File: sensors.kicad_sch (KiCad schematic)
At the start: 17 parts

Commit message: refactor labels U and assigned resistance footprint
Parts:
- R22: footprint (none) -> Resistor_SMD:R_0603_1608Metric
- U4: renamed from U5; value ~ -> SPL06-001
- U5: renamed from U6; value ~ -> ICM-42688-P
- U6: renamed from U8; value ~ -> QMC5883L
- U7: value ~ -> MPU6500
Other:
- moved on the sheet: C30, U5
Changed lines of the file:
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@@
 	(paper "A4")
 	(junction
-		(at 140.97 57.15)
+		(at 163.83 57.15)
 		(diameter 0)
 		(color 0 0 0 0)
 	)
 	(junction
-		(at 140.97 44.45)
+		(at 163.83 44.45)
 		(diameter 0)
 		(color 0 0 0 0)
 	)
 	(junction
-		(at 140.97 60.96)
+		(at 163.83 60.96)
 		(diameter 0)
 		(color 0 0 0 0)
@@
 	)
 	(junction
-		(at 130.81 53.34)
+		(at 153.67 53.34)
 		(diameter 0)
 		(color 0 0 0 0)
@@
 	(wire
 		(pts
-			(xy 140.97 57.15) (xy 140.97 60.96)
+			(xy 163.83 57.15) (xy 163.83 60.96)
 		)
 		(stroke
@@
 	(wire
 		(pts
-			(xy 140.97 45.72) (xy 140.97 44.45)
+			(xy 163.83 45.72) (xy 163.83 44.45)
 		)
 		(stroke
@@
 	(wire
 		(pts
-			(xy 140.97 44.45) (xy 138.43 44.45)
+			(xy 163.83 44.45) (xy 161.29 44.45)
 		)
 		(stroke
@@
 	(wire
 		(pts
-			(xy 142.24 38.1) (xy 144.78 38.1)
+			(xy 165.1 38.1) (xy 167.64 38.1)
 		)
 		(stroke
@@
 	(wire
 		(pts
-			(xy 144.78 60.96) (xy 140.97 60.96)
+			(xy 167.64 60.96) (xy 163.83 60.96)
 		)
 		(stroke
@@
 	(wire
 		(pts
-			(xy 144.78 45.72) (xy 140.97 45.72)
+			(xy 167.64 45.72) (xy 163.83 45.72)
 		)
 		(stroke
@@
 	(wire
 		(pts
-			(xy 130.81 53.34) (xy 144.78 53.34)
+			(xy 153.67 53.34) (xy 167.64 53.34)
 		)
 		(stroke
@@
 	(wire
 		(pts
-			(xy 138.43 57.15) (xy 140.97 57.15)
+			(xy 161.29 57.15) (xy 163.83 57.15)
 		)
 		(stroke
@@
 	(wire
 		(pts
-			(xy 140.97 60.96) (xy 140.97 63.5)
+			(xy 163.83 60.96) (xy 163.83 63.5)
 		)
 		(stroke
@@
 	(wire
 		(pts
-			(xy 140.97 41.91) (xy 140.97 44.45)
+			(xy 163.83 41.91) (xy 163.83 44.45)
 		)
 		(stroke
@@
 	(wire
 		(pts
-			(xy 130.81 53.34) (xy 128.27 53.34)
+			(xy 153.67 53.34) (xy 151.13 53.34)
 		)
 		(stroke
@@
 	(wire
 		(pts
-			(xy 143.51 49.53) (xy 144.78 49.53)
+			(xy 166.37 49.53) (xy 167.64 49.53)
 		)
 		(stroke
@@
 	(wire
 		(pts
-			(xy 144.78 41.91) (xy 140.97 41.91)
+			(xy 167.64 41.91) (xy 163.83 41.91)
 		)
 		(stroke
@@
 	(wire
 		(pts
-			(xy 144.78 57.15) (xy 140.97 57.15)
+			(xy 167.64 57.15) (xy 163.83 57.15)
 		)
 		(stroke
@@
 	(wire
 		(pts
-			(xy 130.81 57.15) (xy 130.81 53.34)
+			(xy 153.67 57.15) (xy 153.67 53.34)
 		)
 		(stroke
@@
 	(global_label "VDD_MCU"
 		(shape input)
-		(at 128.27 53.34 180)
+		(at 151.13 53.34 180)
 		(fields_autoplaced yes)
 		(effects
@@
 		)
 		(property "Intersheetrefs" "${INTERSHEET_REFS}"
-			(at 116.6367 53.34 0)
+			(at 139.4967 53.34 0)
 			(effects
 				(font
@@
 	(global_label "IMU1_SPI4_EXTI2"
 		(shape input)
-		(at 143.51 49.53 180)
+		(at 166.37 49.53 180)
 		(fields_autoplaced yes)
 		(effects
@@
 		)
 		(property "Intersheetrefs" "${INTERSHEET_REFS}"
-			(at 124.5592 49.53 0)
+			(at 147.4192 49.53 0)
 			(effects
 				(font
@@
 	(global_label "SPI4_MISO"
 		(shape input)
-		(at 142.24 38.1 180)
+		(at 165.1 38.1 180)
 		(fields_autoplaced yes)
 		(effects
@@
 		)
 		(property "Intersheetrefs" "${INTERSHEET_REFS}"
-			(at 129.3972 38.1 0)
+			(at 152.2572 38.1 0)
 			(effects
 				(font
@@
 	(symbol
 		(lib_id "power:GND")
-		(at 138.43 44.45 270)
+		(at 161.29 44.45 270)
 		(unit 1)
 		(exclude_from_sim no)
@@
 		(fields_autoplaced yes)
 		(property "Reference" "#PWR026"
-			(at 132.08 44.45 0)
+			(at 154.94 44.45 0)
 			(effects
 				(font
@@
 		)
 		(property "Value" "GND"
-			(at 134.62 44.4499 90)
+			(at 157.48 44.4499 90)
 			(effects
 				(font
@@
 		)
 		(property "Footprint" ""
-			(at 138.43 44.45 0)
+			(at 161.29 44.45 0)
 			(effects
 				(font
@@
 		)
 		(property "Datasheet" ""
-			(at 138.43 44.45 0)
+			(at 161.29 44.45 0)
 			(effects
 				(font
@@
 		)
 		(property "Description" "Power symbol creates a global label with name \"GND\" , ground"
-			(at 138.43 44.45 0)
+			(at 161.29 44.45 0)
 			(effects
 				(font
@@
 		(dnp no)
 		(fields_autoplaced yes)
-		(property "Reference" "U8"
+		(property "Reference" "U6"
 			(at 73.66 99.06 0)
 			(effects
@@
 			)
 		)
-		(property "Value" "~"
+		(property "Value" "QMC5883L"
 			(at 73.66 101.6 0)
 			(effects
@@
 			(project ""
 				(path "/11716af6-0e6e-444b-b738-3f12da23c1a2/8bde1870-17fd-4277-9e11-3b03ad7c1e16"
-					(reference "U8")
+					(reference "U6")
 					(unit 1)
 				)
@@
 	(symbol
 		(lib_id "Device:C")
-		(at 134.62 57.15 90)
+		(at 157.48 57.15 90)
 		(unit 1)
 		(exclude_from_sim no)
@@
 		(dnp no)
 		(property "Reference" "C30"
-			(at 134.62 60.706 90)
+			(at 157.48 60.706 90)
 			(effects
 				(font
@@
 		)
 		(property "Value" "100n"
-			(at 131.064 58.166 90)
+			(at 153.924 58.166 90)
 			(effects
 				(font
@@
 		)
 		(property "Footprint" ""
-			(at 138.43 56.1848 0)
+			(at 161.29 56.1848 0)
 			(effects
 				(font
@@
 		)
 		(property "Datasheet" "~"
-			(at 134.62 57.15 0)
+			(at 157.48 57.15 0)
 			(effects
 				(font
@@
 		)
 		(property "Description" "Unpolarized capacitor"
-			(at 134.62 57.15 0)
+			(at 157.48 57.15 0)
 			(effects
 				(font
@@
 		(dnp no)
 		(fields_autoplaced yes)
-		(property "Reference" "U5"
+		(property "Reference" "U4"
 			(at 65.405 34.29 0)
 			(effects
@@
 			)
 		)
-		(property "Value" "~"
+		(property "Value" "SPL06-001"
 			(at 65.405 36.83 0)
 			(effects
@@
 			(project ""
 				(path "/11716af6-0e6e-444b-b738-3f12da23c1a2/8bde1870-17fd-4277-9e11-3b03ad7c1e16"
-					(reference "U5")
+					(reference "U4")
 					(unit 1)
 				)
@@
 	(symbol
 		(lib_id "power:GND")
-		(at 140.97 63.5 0)
+		(at 163.83 63.5 0)
 		(unit 1)
 		(exclude_from_sim no)
@@
 		(fields_autoplaced yes)
 		(property "Reference" "#PWR025"
-			(at 140.97 69.85 0)
+			(at 163.83 69.85 0)
 			(effects
 				(font
@@
 		)
 		(property "Value" "GND"
-			(at 140.97 68.58 0)
+			(at 163.83 68.58 0)
 			(effects
 				(font
@@
 		)
 		(property "Footprint" ""
-			(at 140.97 63.5 0)
+			(at 163.83 63.5 0)
 			(effects
 				(font
@@
 		)
 		(property "Datasheet" ""
-			(at 140.97 63.5 0)
+			(at 163.83 63.5 0)
 			(effects
 				(font
@@
 		)
 		(property "Description" "Power symbol creates a global label with name \"GND\" , ground"
-			(at 140.97 63.5 0)
+			(at 163.83 63.5 0)
 			(effects
 				(font
@@
 	(symbol
 		(lib_id "fclib:ICM42688P")
-		(at 146.05 33.02 0)
+		(at 194.31 50.8 0)
 		(unit 1)
 		(exclude_from_sim no)
@@
 		(dnp no)
 		(fields_autoplaced yes)
-		(property "Reference" "U6"
-			(at 183.515 29.21 0)
+		(property "Reference" "U5"
+			(at 194.818 31.496 0)
 			(effects
 				(font
@@
 			)
 		)
-		(property "Value" "~"
-			(at 183.515 31.75 0)
+		(property "Value" "ICM-42688-P"
+			(at 195.072 33.274 0)
 			(effects
 				(font
@@
 		)
 		(property "Footprint" ""
-			(at 146.05 33.02 0)
+			(at 194.31 50.8 0)
 			(effects
 				(font
@@
 		)
 		(property "Datasheet" ""
-			(at 146.05 33.02 0)
+			(at 194.31 50.8 0)
 			(effects
 				(font
@@
 		)
 		(property "Description" ""
-			(at 146.05 33.02 0)
+			(at 194.31 50.8 0)
 			(effects
 				(font
@@
 			(project ""
 				(path "/11716af6-0e6e-444b-b738-3f12da23c1a2/8bde1870-17fd-4277-9e11-3b03ad7c1e16"
-					(reference "U6")
+					(reference "U5")
 					(unit 1)
 				)
@@
 			)
 		)
-		(property "Value" "~"
+		(property "Value" "MPU6500"
 			(at 194.31 88.9 0)
 			(effects
@@
 			)
 		)
-		(property "Footprint" ""
+		(property "Footprint" "Resistor_SMD:R_0603_1608Metric"
 			(at 75.692 52.07 90)
 			(effects

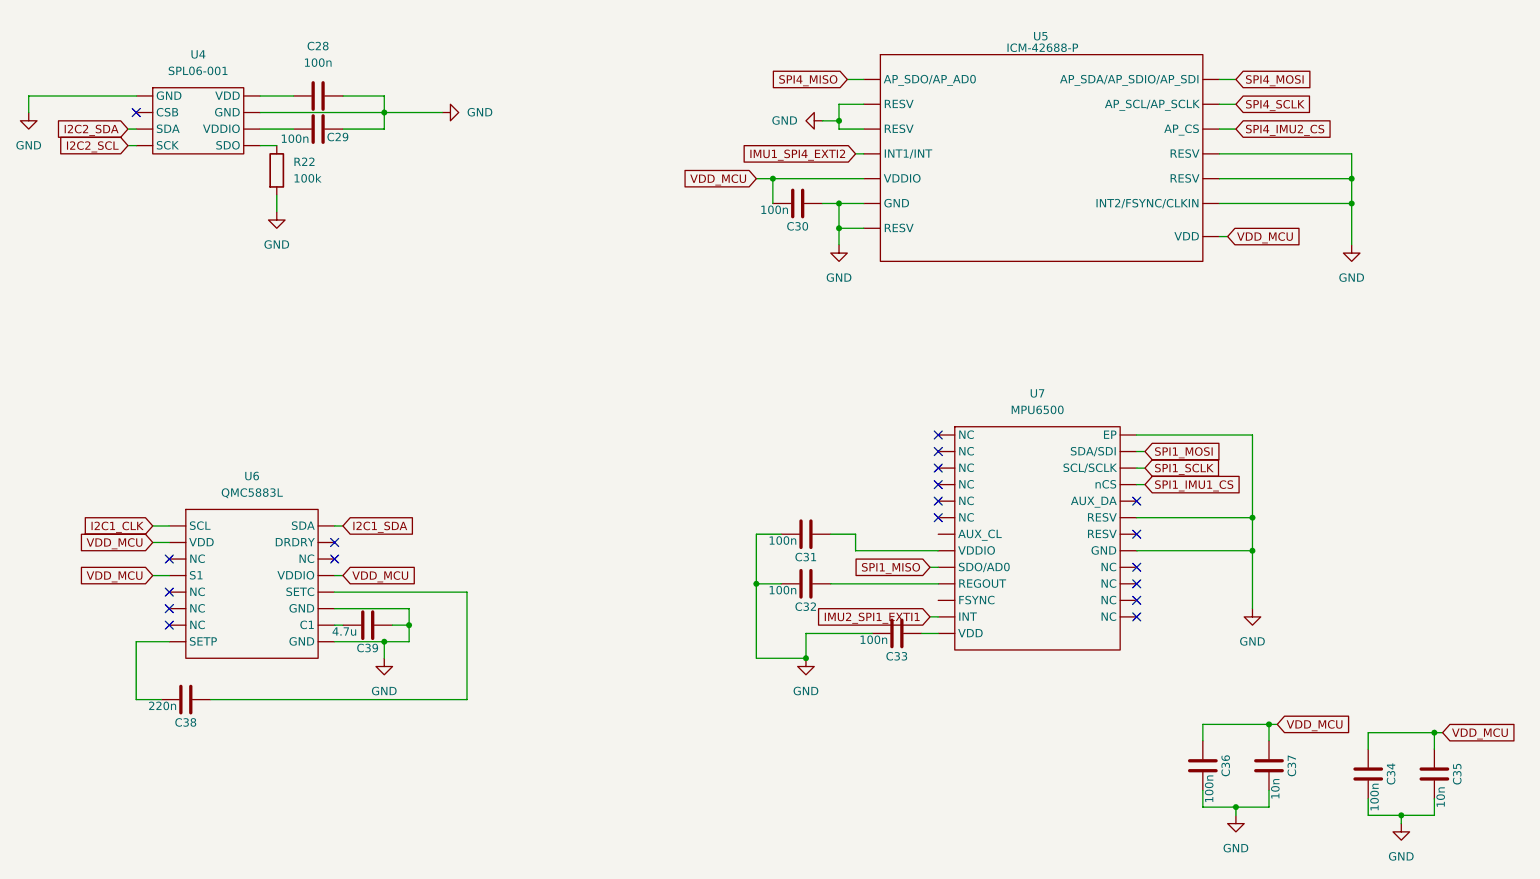
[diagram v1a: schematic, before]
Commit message: refactor and update references, added some footprints
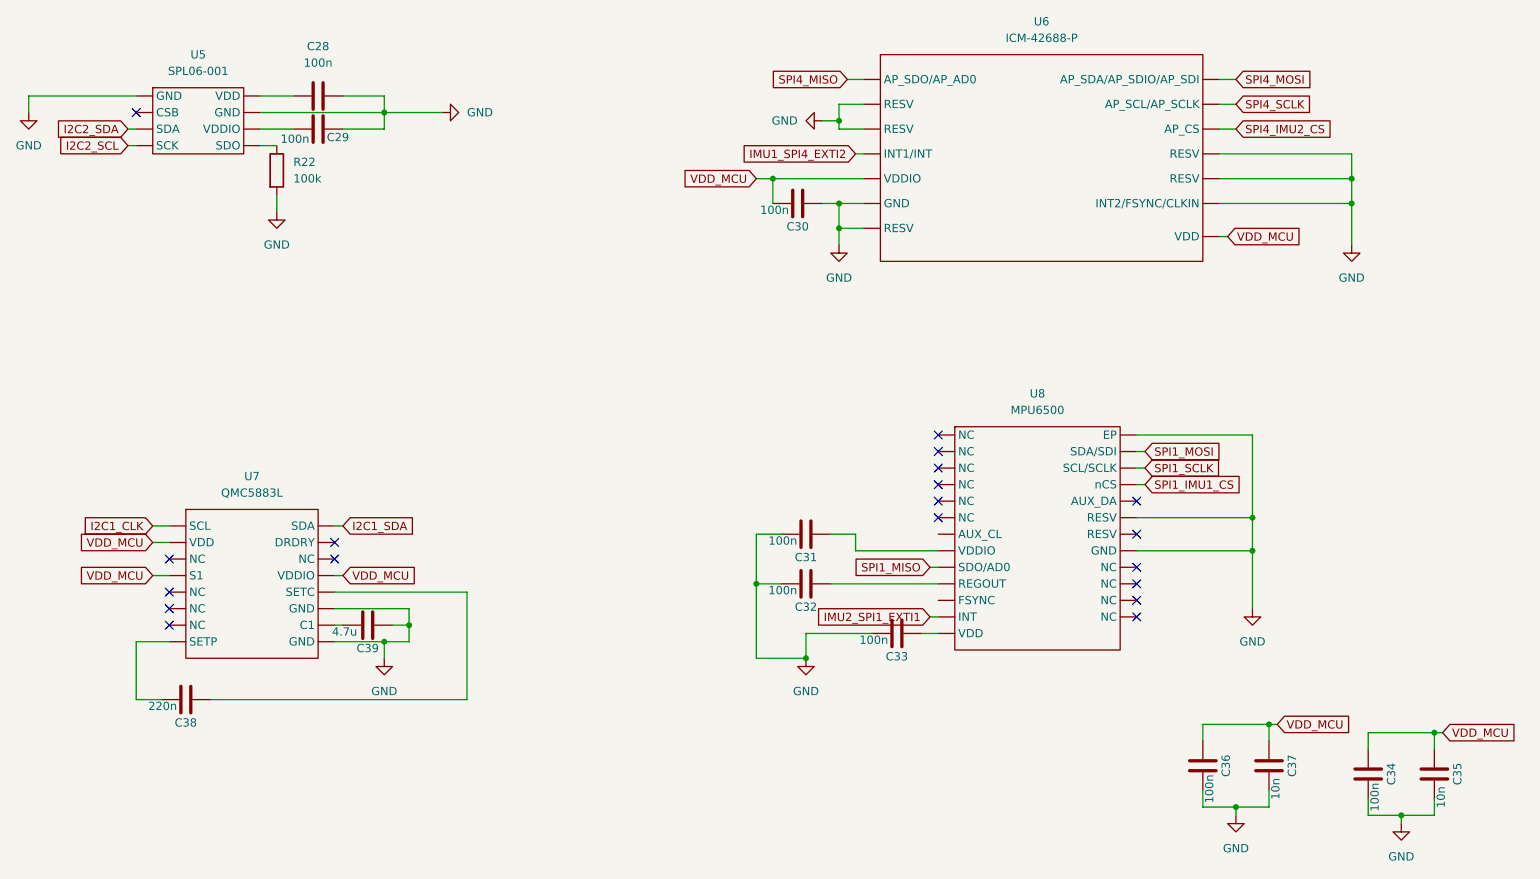
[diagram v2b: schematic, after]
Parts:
- C28, C29, C30, C31, C32, C33, C34, C35, C36, C37, C38: footprint (none) -> Capacitor_SMD:C_0603_1608Metric
- C39: footprint (none) -> Capacitor_SMD:C_0805_2012Metric
- renumbered U4 to U5, U5 to U6, U6 to U7, U7 to U8
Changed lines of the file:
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@@
 			)
 		)
-		(property "Footprint" ""
+		(property "Footprint" "Capacitor_SMD:C_0603_1608Metric"
 			(at 87.63 44.7548 0)
 			(effects
@@
 			)
 		)
-		(property "Footprint" ""
+		(property "Footprint" "Capacitor_SMD:C_0603_1608Metric"
 			(at 162.56 114.6048 0)
 			(effects
@@
 		(dnp no)
 		(fields_autoplaced yes)
-		(property "Reference" "U6"
+		(property "Reference" "U7"
 			(at 73.66 99.06 0)
 			(effects
@@
 			(project ""
 				(path "/11716af6-0e6e-444b-b738-3f12da23c1a2/8bde1870-17fd-4277-9e11-3b03ad7c1e16"
-					(reference "U6")
+					(reference "U7")
 					(unit 1)
 				)
@@
 			)
 		)
-		(property "Footprint" ""
+		(property "Footprint" "Capacitor_SMD:C_0603_1608Metric"
 			(at 162.56 106.9848 0)
 			(effects
@@
 			)
 		)
-		(property "Footprint" ""
+		(property "Footprint" "Capacitor_SMD:C_0603_1608Metric"
 			(at 67.31 132.3848 0)
 			(effects
@@
 			)
 		)
-		(property "Footprint" ""
+		(property "Footprint" "Capacitor_SMD:C_0603_1608Metric"
 			(at 176.53 122.2248 0)
 			(effects
@@
 			)
 		)
-		(property "Footprint" ""
+		(property "Footprint" "Capacitor_SMD:C_0603_1608Metric"
 			(at 244.1448 140.97 0)
 			(effects
@@
 			)
 		)
-		(property "Footprint" ""
+		(property "Footprint" "Capacitor_SMD:C_0603_1608Metric"
 			(at 161.29 56.1848 0)
 			(effects
@@
 			)
 		)
-		(property "Footprint" ""
+		(property "Footprint" "Capacitor_SMD:C_0603_1608Metric"
 			(at 218.7448 139.7 0)
 			(effects
@@
 			)
 		)
-		(property "Footprint" ""
+		(property "Footprint" "Capacitor_SMD:C_0805_2012Metric"
 			(at 95.25 120.9548 0)
 			(effects
@@
 			)
 		)
-		(property "Footprint" ""
+		(property "Footprint" "Capacitor_SMD:C_0603_1608Metric"
 			(at 87.63 39.6748 0)
 			(effects
@@
 		(dnp no)
 		(fields_autoplaced yes)
-		(property "Reference" "U4"
+		(property "Reference" "U5"
 			(at 65.405 34.29 0)
 			(effects
@@
 			(project ""
 				(path "/11716af6-0e6e-444b-b738-3f12da23c1a2/8bde1870-17fd-4277-9e11-3b03ad7c1e16"
-					(reference "U4")
+					(reference "U5")
 					(unit 1)
 				)
@@
 		(dnp no)
 		(fields_autoplaced yes)
-		(property "Reference" "U5"
-			(at 194.818 31.496 0)
+		(property "Reference" "U6"
+			(at 194.945 29.21 0)
 			(effects
 				(font
@@
 		)
 		(property "Value" "ICM-42688-P"
-			(at 195.072 33.274 0)
+			(at 194.945 31.75 0)
 			(effects
 				(font
@@
 			(project ""
 				(path "/11716af6-0e6e-444b-b738-3f12da23c1a2/8bde1870-17fd-4277-9e11-3b03ad7c1e16"
-					(reference "U5")
+					(reference "U6")
 					(unit 1)
 				)
@@
 			)
 		)
-		(property "Footprint" ""
+		(property "Footprint" "Capacitor_SMD:C_0603_1608Metric"
 			(at 228.9048 139.7 0)
 			(effects
@@
 		(dnp no)
 		(fields_autoplaced yes)
-		(property "Reference" "U7"
+		(property "Reference" "U8"
 			(at 194.31 86.36 0)
 			(effects
@@
 			(project ""
 				(path "/11716af6-0e6e-444b-b738-3f12da23c1a2/8bde1870-17fd-4277-9e11-3b03ad7c1e16"
-					(reference "U7")
+					(reference "U8")
 					(unit 1)
 				)
@@
 			)
 		)
-		(property "Footprint" ""
+		(property "Footprint" "Capacitor_SMD:C_0603_1608Metric"
 			(at 254.3048 140.97 0)
 			(effects
